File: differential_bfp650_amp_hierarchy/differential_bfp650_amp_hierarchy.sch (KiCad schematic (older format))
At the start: 19 parts

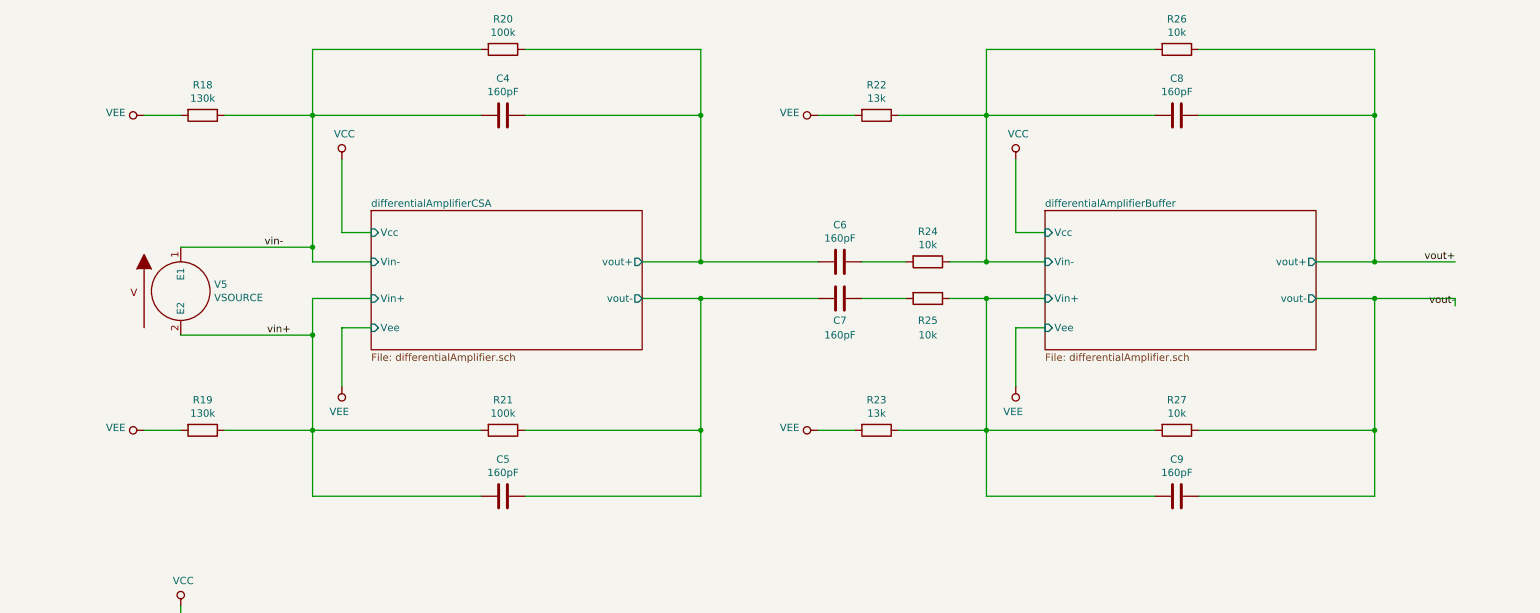
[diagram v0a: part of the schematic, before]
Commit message: Bug fixes to SiPMT_model2.cir ( had to hack to work with NGSpice then fix bugs in hacks... )
TODO:

1) Check size of output signal - is the SiPM delivering the correct amount of charge?

2) Tune R,C to get a bipolar shape ( needed for powering amplifier over signal wires )
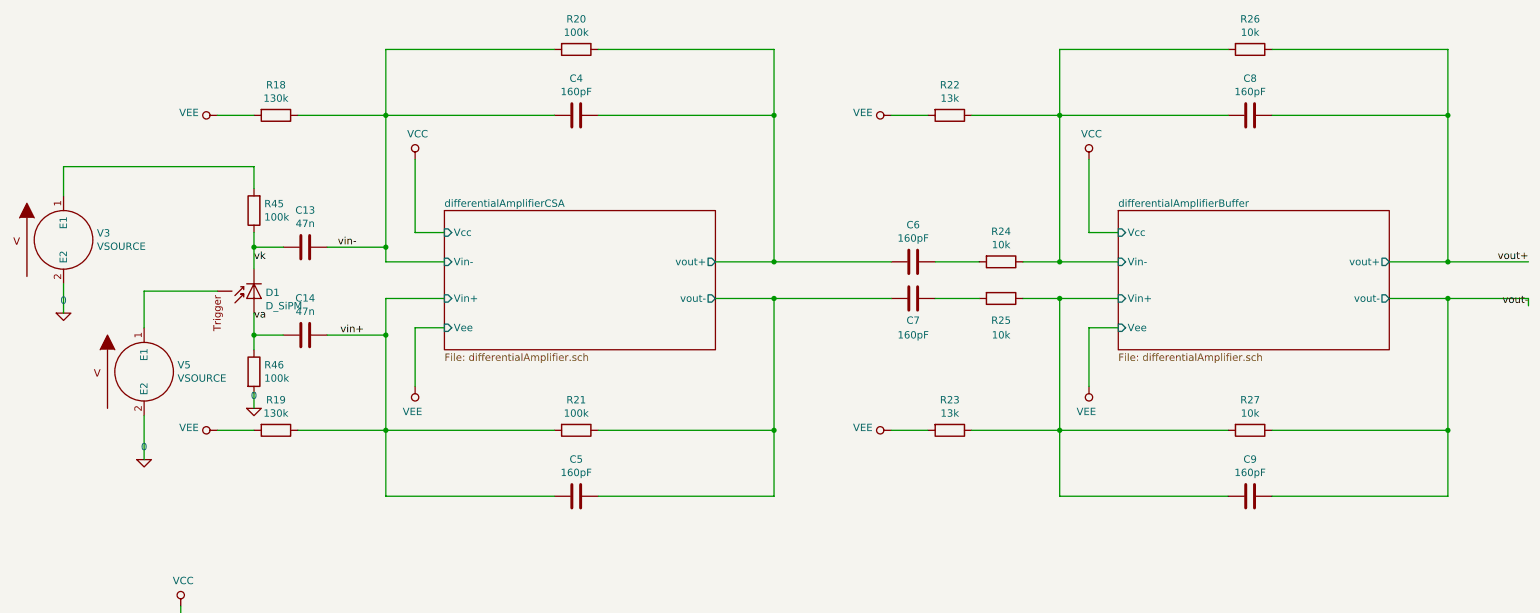
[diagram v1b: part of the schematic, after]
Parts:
- added C13, C14: 47n, symbol Device:C
- added D1: D_SiPM, symbol d_sipm:D_SiPM
- added R45, R46: 100k, symbol Device:R
- added V3: VSOURCE, symbol pspice:VSOURCE
- V5: Spice_Model dc 0 ac 10u pulse(0 1m 50n 10n 10n 50n) -> dc 0 ac 0 pulse(0V 1V 50n 1n 1n 1n)
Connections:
- net 0: now also V5.2 (E2), R46.2, V3.2 (E2)
- net vin+: now also C14.1; no longer V5.2 (E2)
- net vin-: now also C13.1; no longer V5.1 (E1)
- new net: D1.3 (trigger), V5.1 (E1)
- new net: R45.2, V3.1 (E1)
- new net va: C14.2, D1.1 (A), R46.1
- new net vk: C13.2, D1.2 (K), R45.1
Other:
- moved on the sheet: C4, C5, C6, C7, C8, C9, R18, R19, R20, R21, R22, R23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

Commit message: Tuned simulation. Added extra RC in collector of differential amplifier output buffer. Tuned values to restore stability
Simulating 10 SiPM in parallel by increasing number of pixels x10 w.r.t.
model of single 3x3mm^2 SiPM

Peaking time ~ 800ns
Gain ~ 1 mV per Pixel Avalanche.
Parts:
- added C24, C25, C28, C29, C30: 100n, symbol Device:C
- added C26, C27: 10u, symbol Device:C
- added L1, L2, L3, L4: 100uH, symbol Device:L
- added R47, R48, R72, R73: 50, symbol Device:R
- added R74, R75: 100k, symbol Device:R
- added V4, V6: VSOURCE, symbol pspice:VSOURCE
- C6, C7: value 160pF -> 800pF
- C8, C9: value 160pF -> 80pF
- R22, R23: value 13k -> 25k
- R24, R25: value 10k -> 2k
- R26, R27: value 10k -> 21.5k
- V3: Spice_Model 72.0 -> dc 72.0
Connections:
- net 0: now also C26.2, C27.2, C30.1, R72.2, R73.1, V4.2 (E2), V6.1 (E1); no longer V1.2 (E2), V2.1 (E1)
- net VCC: now also V4.1 (E1); no longer V1.1 (E1)
- net VEE: now also V6.2 (E2); no longer V2.2 (E2)
- net vout+: now also C28.2, R48.1; no longer C8.1, R26.1
- net vout-: now also C29.2, R47.1; no longer C9.1, R27.1
- net at V3.1 (E1): now also V1.2 (E2), V2.1 (E1); no longer R45.2
- net differentialAmplifierBuffer/Vin+ renamed vbufin-
- net differentialAmplifierBuffer/Vin- renamed vbufin+
- net differentialAmplifierCSA/vout+ renamed vcsa0+
- net differentialAmplifierCSA/vout- renamed vcsa0-
- new net: L3.1, V1.1 (E1)
- new net: L4.1, V2.2 (E2)
- new net HT: C30.2, R45.2, R74.2, R75.2
- new net dummyVcc: C26.1, L1.1, R74.1
- new net dummyVee: C27.1, L2.1, R75.1
- new net vbufout+: C9.1, R27.1, R48.2
- new net vbufout-: C8.1, R26.1, R47.2
- new net vline+: C24.2, C28.1, L1.2, L3.2
- new net vline-: C25.2, C29.1, L2.2, L4.2
- new net vrx+: C24.1, R72.1
- new net vrx-: C25.1, R73.2
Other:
- note added: "+PSPICE\n.control\noptions savecurrent\ntran 5ns 5us\nwrite\n.endc"
- note added: "In a real circuit, dummyVcc and dummyVee would be used\nas the supply for the amplifier. Unfortunately NGSpice won't converge\nif this is done in simulation"
- note added: "Shielded pair \nwith ground wire"
- note added: "This circuitry represents power and SiPM bias voltage being sent down\na shielded twisted pair cable\n"
- note added: "V5 represents a pulse of light\nthat triggers the SiPM\n(causes switch to close inside model)"
- note added: "v1,v2 are the low voltage supplies\nfor the amplifier\nv3 is the bias for the SiPMs"
- note added: "vrx+ and vrx- are the output to the amplifier/digitizer"
- note removed: "+PSPICE\n.control\ntran 1ns 500ns\nwrite\n.endc"
- moved on the sheet: V1, V2

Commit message: More hacking to get circuit stable at -186 degC ( still slight ringing )
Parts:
- added C19, C20: 47n, symbol Device:C
- added C21, C22: 160pF, symbol Device:C
- added C23, C31: 800pF, symbol Device:C
- added C37: 3.2n, symbol Device:C
- added R53, R54, R57, R58: 100k, symbol Device:R
- added R55, R56: 130k, symbol Device:R
- added R59, R60: 2k, symbol Device:R
- D1: Spice_Model SiPMT -> SiPMT Nf=100
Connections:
- net 0: now also R54.2
- net HT: now also R53.2
- net VEE: now also R55.2, R56.2
- net vbufin+: now also R59.1
- net vbufin-: now also R60.1
- new net: C23.1, R59.2
- new net: C31.1, R60.2
- new net va1: C20.2, C37.2, R54.1
- new net vcsa1+: C21.1, C23.2, R57.1
- new net vcsa1-: C22.1, C31.2, R58.1
- new net vin1+: C20.1, C22.2, R56.1, R58.2
- new net vin1-: C19.1, C21.2, R55.1, R57.2
- new net vk1: C19.2, C37.1, R53.1
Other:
- note added: "+PSPICE\n.control\noptions savecurrent\n* Hack reltol to get NGSpice to converge\noptions reltol=0.005\noptions temp=-186\ntran 5ns 5us\nplot v("/vrx+") v("/vrx-")\nplot v("/differentialAmplifierBuffer/vbuf1")\nplot v("/differentialAmplifierBuffer/vcoutm")\nplot i(l.xu7.lc) i(l.xu12.lc)\nplot i(l.xu7.le) i(l.xu12.le)\nwrite\n.endc"
- note added: "3.2nF capacitor is a crude \nmodel of 10 3x3mm SiPM in\nparallel"
- note added: "Differential Cryogenic Pre-amplifier for SiPM\nDifferential signal of approximately \n1mV / Pixel Avalanche"
- note added: "V4 and V6 are for simulation only.\nIn a real circuit, power for amplifier \nsupplied down cable\n( NGSpice convergence problems if power\nsimulation down cable )"
- note removed: "+PSPICE\n.control\noptions savecurrent\ntran 5ns 5us\nwrite\n.endc"
